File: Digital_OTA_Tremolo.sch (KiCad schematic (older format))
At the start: 25 parts

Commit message: updates
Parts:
- added R?: 10K, symbol Device:R
- added RV?: 47K, symbol Device:R_POT_TRIM
- R?: value 33K -> 4K7
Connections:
- net labels added: CV
- net labels removed: DAC1
- wire segments 95 -> 106
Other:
- moved on the sheet: R?
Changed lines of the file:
@@
 L Digital_OTA_Tremolo-rescue:R R?
 U 1 1 5AD2DE34
-P 6200 3800
-F 0 "R?" V 6280 3800 50  0000 C CNN
-F 1 "33K" V 6200 3800 50  0000 C CNN
-F 2 "" V 6130 3800 50  0001 C CNN
-F 3 "" H 6200 3800 50  0001 C CNN
-	1    6200 3800
+P 5825 3800
+F 0 "R?" V 5905 3800 50  0000 C CNN
+F 1 "4K7" V 5825 3800 50  0000 C CNN
+F 2 "" V 5755 3800 50  0001 C CNN
+F 3 "" H 5825 3800 50  0001 C CNN
+	1    5825 3800
 	0    1    1    0
 $EndComp
@@
 	10900 3500 11450 3500
 Wire Wire Line
-	5400 3800 6050 3800
+	5400 3800 5675 3800
 $Comp
 L Device:R_POT_TRIM RV?
@@
 	9550 3500 9900 3500
 Wire Wire Line
-	8825 3500 9550 3500
+	8825 3500 9275 3500
 Wire Wire Line
 	10200 3800 10200 3975
@@
 	1    0    0    -1
 $EndComp
-Wire Wire Line
-	6350 3800 6900 3800
-Connection ~ 6900 3800
 $Comp
 L Device:D D?
@@
 Wire Wire Line
 	11750 3500 12300 3500
-Wire Wire Line
-	8825 3600 9025 3600
 $Comp
 L MCU_ST_STM32F0:STM32F051K8Tx U?
@@
 $EndComp
 Wire Wire Line
-	4525 6875 9025 6875
-Wire Wire Line
-	9025 6875 9025 3600
-Text Label 6025 6875 0    50   ~ 0
-DAC1
-Text Notes 6025 6975 0    50   ~ 0
+	4525 6875 5500 6875
+Text Notes 4650 6975 0    50   ~ 0
 SINE WAVE < 30Hz\n
 $Comp
@@
 Wire Wire Line
 	6525 7575 6525 7275
+Wire Wire Line
+	6900 3200 6175 3200
+Wire Wire Line
+	6175 3200 6175 3800
+Wire Wire Line
+	6175 3800 5975 3800
+Connection ~ 6900 3200
+Wire Wire Line
+	8825 3600 9075 3600
+Text Label 9075 3600 2    50   ~ 0
+CV
+Text Label 6475 6875 2    50   ~ 0
+CV
+Wire Wire Line
+	9275 3500 9275 4350
+Wire Wire Line
+	9275 4350 8850 4350
+Wire Wire Line
+	8100 4350 8100 3800
+Connection ~ 9275 3500
+Wire Wire Line
+	9275 3500 9550 3500
+Connection ~ 8100 3800
+$Comp
+L Device:R R?
+U 1 1 5E90DE19
+P 8700 4350
+F 0 "R?" V 8493 4350 50  0000 C CNN
+F 1 "10K" V 8584 4350 50  0000 C CNN
+F 2 "" V 8630 4350 50  0001 C CNN
+F 3 "~" H 8700 4350 50  0001 C CNN
+	1    8700 4350
+	0    1    1    0
+$EndComp
+Wire Wire Line
+	8550 4350 8100 4350
+$Comp
+L Device:R_POT_TRIM RV?
+U 1 1 5E9351EC
+P 5875 6875
+F 0 "RV?" V 5760 6875 50  0000 C CNN
+F 1 "47K" V 5669 6875 50  0000 C CNN
+F 2 "" H 5875 6875 50  0001 C CNN
+F 3 "~" H 5875 6875 50  0001 C CNN
+	1    5875 6875
+	0    -1   -1   0
+$EndComp
+Wire Wire Line
+	6025 6875 6475 6875
+Wire Wire Line
+	5875 6725 5875 6675
+Wire Wire Line
+	5875 6675 5500 6675
+Wire Wire Line
+	5500 6675 5500 6875
+Connection ~ 5500 6875
+Wire Wire Line
+	5500 6875 5725 6875
 $EndSCHEMATC

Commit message: updates
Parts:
- removed R? (x2): 10k, symbol Device:R
- removed RV?: 47K, symbol Device:R_POT_TRIM
- removed SW?: Rotary_Encoder, symbol Device:Rotary_Encoder
- removed U? (x2): LM833, symbol Digital_OTA_Tremolo-rescue:TL074
- removed U?: STM32F051K8Tx, Package_QFP:LQFP-32_7x7mm_P0.8mm, symbol MCU_ST_STM32F0:STM32F051K8Tx
- added C? (x4): C, symbol Device:C
- added D?: 1N914, symbol Device:D
- added D? (x2): LED, symbol Device:LED
- added R? (x3): 10K, symbol Digital_OTA_Tremolo-rescue:R
- added R? (x2): 10K, symbol Device:R
- added R?: 33K, symbol Digital_OTA_Tremolo-rescue:R
- added R?: 4K7, symbol Digital_OTA_Tremolo-rescue:R
- added R? (x3): 1K, symbol Digital_OTA_Tremolo-rescue:R
- added R? (x2): 1K, symbol Device:R
- added R? (x2): 2K7, symbol Digital_OTA_Tremolo-rescue:R
- added R? (x2): 33K, symbol Device:R
- added RV? (x2): B10K, symbol Device:R_POT
- added U? (x6): TL072, symbol Amplifier_Operational:TL072
- added U?: STM32F072RBTx, Package_QFP:LQFP-64_10x10mm_P0.5mm, symbol MCU_ST_STM32F0:STM32F072RBTx
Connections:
- net labels added: +3V3, CV1, CV2, INV_CV1, INV_CV2, InvertInput, NonInvInput, RATE1, RATE2
- net labels removed: CV
- wire segments 106 -> 194
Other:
- note added: "3.7 Gain"
- note added: "DAC: Channel 1 + 2\nSINE WAVE < 100Hz\n"
- note removed: "SINE WAVE < 30Hz\n"
- moved on the sheet: C?, D?, J?, R?, RV?, U?, U?A, U?B, U?C, U?D

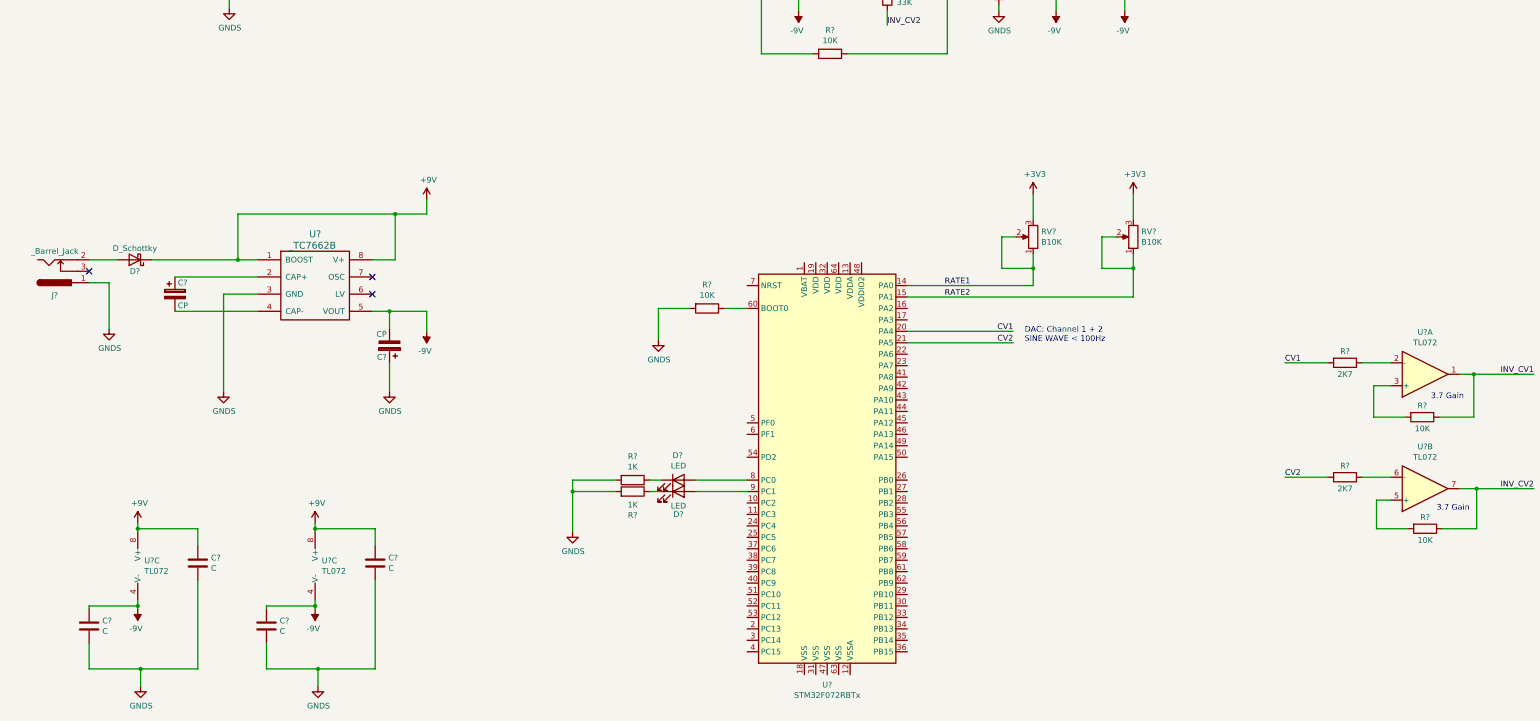
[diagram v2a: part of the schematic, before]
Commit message: updated schema
_ added controls
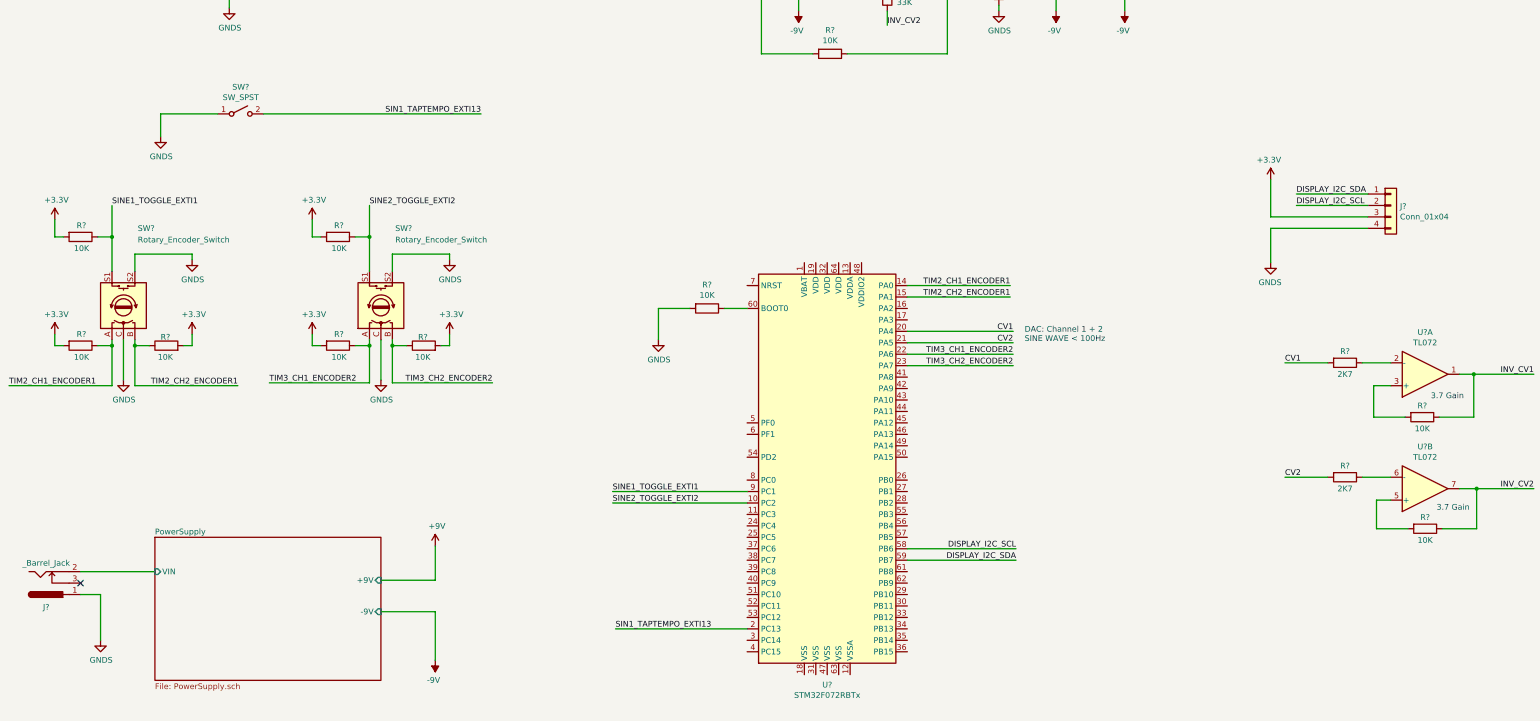
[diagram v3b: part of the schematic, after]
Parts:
- removed C? (x2): CP, symbol Digital_OTA_Tremolo-rescue:CP
- removed C? (x4): C, symbol Device:C
- removed D?: D_Schottky, symbol Digital_OTA_Tremolo-rescue:D_Schottky
- removed D? (x2): LED, symbol Device:LED
- removed J?: _Barrel_Jack, symbol barrel_jack:_Barrel_Jack
- removed R? (x2): 1K, symbol Device:R
- removed RV? (x2): B10K, symbol Device:R_POT
- removed U?: _TC7662B, symbol _TC7662b:_TC7662B
- removed U? (x2): TL072, symbol Amplifier_Operational:TL072
- added J?: _Barrel_Jack, symbol barrel_jack:_Barrel_Jack
- added J?: Conn_01x04, symbol Connector_Generic:Conn_01x04
- added R? (x6): 10K, symbol Device:R
- added SW? (x2): Rotary_Encoder_Switch, symbol Device:Rotary_Encoder_Switch
- added SW?: SW_SPST, symbol Switch:SW_SPST
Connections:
- net +3V3: now also J?.3 (Pin_3), R?.2, R?.2, R?.2, R?.2, R?.2, R?.2
- net GNDS: now also J?.1, J?.4 (Pin_4), SW?.1 (A), SW?.C, SW?.C, SW?.S2, SW?.S2
- net SINE1_TOGGLE_EXTI1: now reaches U?.9 (PC1)
- net SINE1_TOGGLE_EXTI1: now also R?.1, SW?.S1
- net SINE2_TOGGLE_EXTI2: now reaches U?.10 (PC2)
- net SINE2_TOGGLE_EXTI2: now also R?.1, SW?.S1
- net SIN1_TAPTEMPO_EXTI13: now reaches U?.2 (PC13)
- net SIN1_TAPTEMPO_EXTI13: now also SW?.2 (B)
- net TIM3_CH1_ENCODER2: now reaches U?.22 (PA6)
- net TIM3_CH1_ENCODER2: now also R?.1, SW?.A
- net TIM3_CH2_ENCODER2: now reaches U?.23 (PA7)
- net TIM3_CH2_ENCODER2: now also R?.1, SW?.B
- net DISPLAY_I2C_SCL: now reaches U?.58 (PB6)
- net DISPLAY_I2C_SCL: now also J?.2 (Pin_2)
- net DISPLAY_I2C_SDA: now reaches U?.59 (PB7)
- net DISPLAY_I2C_SDA: now also J?.1 (Pin_1)
- net RATE1 renamed TIM2_CH1_ENCODER1
- net TIM2_CH1_ENCODER1: now also R?.1, SW?.A
- net RATE2 renamed TIM2_CH2_ENCODER1
- net TIM2_CH2_ENCODER1: now also R?.1, SW?.B
- new net PowerSupply/VIN: J?.2
- no-connect marks 5 -> 3

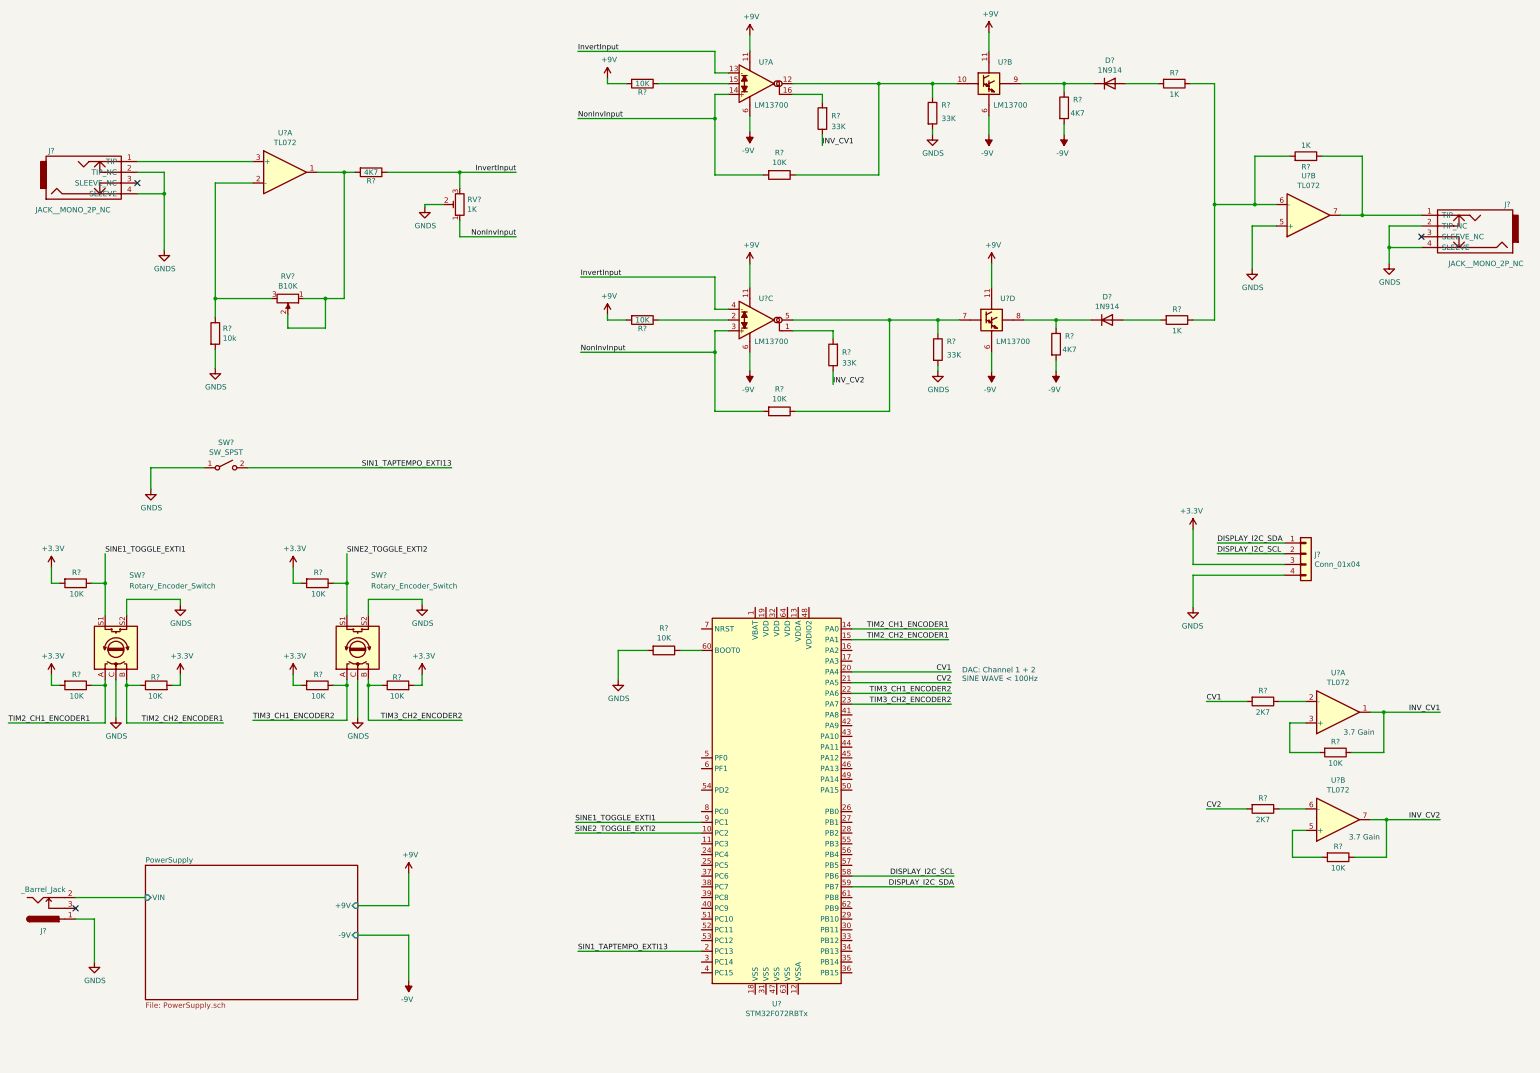
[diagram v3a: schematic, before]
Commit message: Updated power supply section
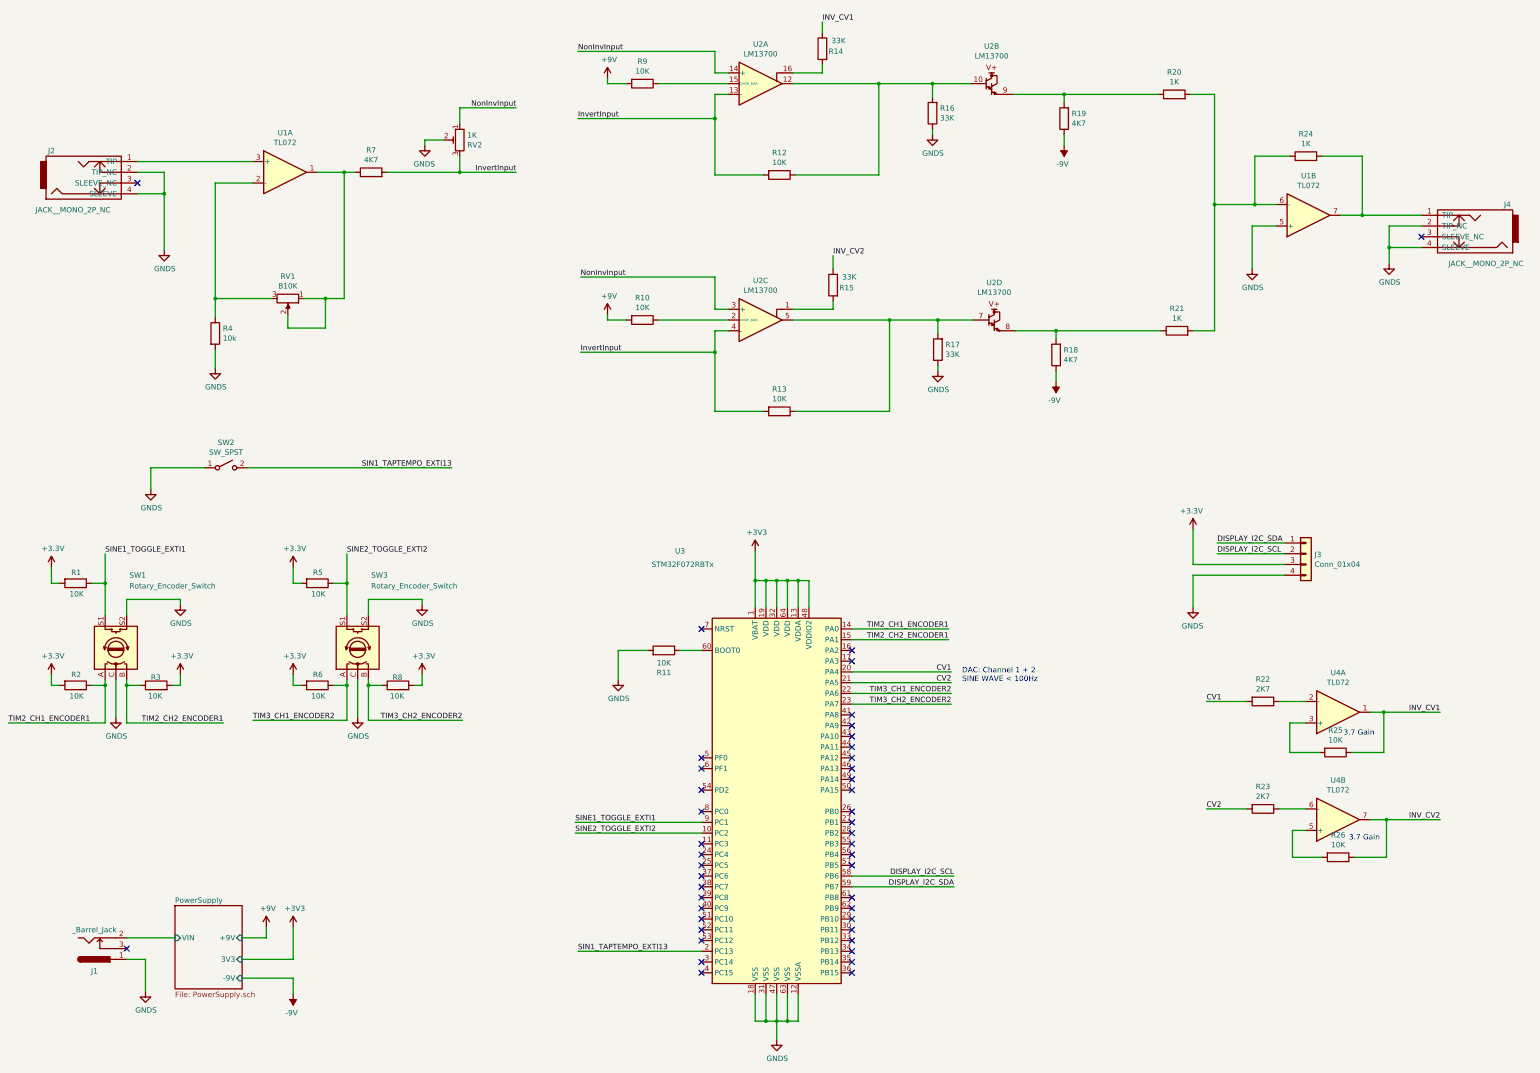
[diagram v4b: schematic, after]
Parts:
- removed D? (x2): 1N914, symbol Device:D
- removed R? (x4): 10K, symbol Digital_OTA_Tremolo-rescue:R
- removed R? (x3): 4K7, symbol Digital_OTA_Tremolo-rescue:R
- removed R? (x2): 33K, symbol Digital_OTA_Tremolo-rescue:R
- removed R? (x3): 1K, symbol Digital_OTA_Tremolo-rescue:R
- removed R? (x2): 2K7, symbol Digital_OTA_Tremolo-rescue:R
- removed U? (x4): LM13700, symbol Digital_OTA_Tremolo-rescue:LM13700
- added R10, R25, R26, R9: 10K, symbol Device:R
- added R16, R17: 33K, symbol Device:R
- added R18, R19, R7: 4K7, symbol Device:R
- added R20, R21, R24: 1K, symbol Device:R
- added R22, R23: 2K7, symbol Device:R
- added U2: LM13700, symbol Amplifier_Operational:LM13700
- gave numbers to parts that had none: 24
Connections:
- net +3V3: now also U3.1 (VBAT), U3.13 (VDDA), U3.19 (VDD), U3.32 (VDD), U3.48 (VDDIO2), U3.64 (VDD)
- net +9V: now also R10.2, R9.2
- net -9V: now also R18.1, R19.1
- net CV1: now also R22.2
- net CV2: now also R23.2
- net GNDS: now also U3.12 (VSSA), U3.18 (VSS), U3.31 (VSS), U3.47 (VSS), U3.63 (VSS), R16.1, R17.1
- net INV_CV1: now also R25.1
- net INV_CV2: now also R26.1
- net InvertInput: now also R12.2, R13.2, R7.2, U2.13 (-), U2.4 (-)
- net NonInvInput: now also U2.14 (+), U2.3 (+); no longer R12.2, R13.2
- net at R12.1: now also R16.2, U2.10, U2.12
- net at R14.2: now also U2.16
- net at R15.2: now also U2.1
- net at R13.1: now also R17.2, U2.5, U2.7
- net at J4.1 (TIP), U1.7: now also R24.2
- net at RV1.1, RV1.2, U1.1: now also R7.1
- net at U1.6 (-): now also R20.2, R21.2, R24.1
- net at U4.2 (-): now also R22.1
- net at U4.3 (+): now also R25.2
- net at U4.5 (+): now also R26.2
- net at U4.6 (-): now also R23.1
- new net: R9.1, U2.15 (DIODE_BIAS)
- new net: R19.2, R20.1, U2.9
- new net: R10.1, U2.2 (DIODE_BIAS)
- new net: R18.2, R21.1, U2.8
- no-connect marks 3 -> 44
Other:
- moved on the sheet: J1, R14, R15, RV2

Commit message: Updated RevA design
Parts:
- removed J1: _Barrel_Jack, symbol barrel_jack:_Barrel_Jack
- removed J2, J4: JACK__MONO_2P_NC, symbol socket_custom:JACK__MONO_2P_NC
- removed RV1: B10K, symbol pot_numbered:NPOT
- removed U1, U4: TL072, symbol Amplifier_Operational:TL072
- added J1, J4: NRJ6HM-1-PRE, NeutrikNRJ:NRJxHx, symbol MonoJack2Switch:MonoJack2Switch
- added J2: Barrel_Jack_Switch, Connector_BarrelJack:BarrelJack_Horizontal, symbol Connector:Barrel_Jack_Switch
- added RV1: B10K, Potentiometer_THT:Potentiometer_Bourns_PTV09A-1_Single_Vertical, symbol Device:R_POT
- added U1: TL074, Package_SO:SOIC-16_3.9x9.9mm_P1.27mm, symbol Amplifier_Operational:TL074
- J3: footprint (none) -> Connector_Molex:Molex_KK-254_AE-6410-04A_1x04_P2.54mm_Vertical
- R1, R10, R11, R12, R13, R14, R15, R16, R17, R18, R19, R2, R20, R21, R22, R23, R24, R25, R26, R3, R4, R5, R6, R7, R8, R9: footprint (none) -> Resistor_SMD:R_0805_2012Metric_Pad1.15x1.40mm_HandSolder
- RV2: footprint (none) -> Potentiometer_SMD:Potentiometer_Bourns_3314J_Vertical
- SW1, SW3: footprint (none) -> Rotary_Encoder:RotaryEncoder_Alps_EC11E-Switch_Vertical_H20mm
- SW2: footprint (none) -> Connector_Molex:Molex_KK-254_AE-6410-02A_1x02_P2.54mm_Vertical
- U2: footprint (none) -> Package_SO:SOIC-16_3.9x9.9mm_P1.27mm
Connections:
- net INV_CV1: now also U1.8
- net INV_CV2: now also U1.14
- net at R24.2: now also J4.1 (TIP), U1.7
- net at R4.1: now also RV1.3, U1.2 (-)
- net at R7.1: now also RV1.1, RV1.2, U1.1
- net at R20.2, R21.2, R24.1: now also U1.6 (-)
- net at R26.2: now also U1.12 (+)
- net at R25.2: now also U1.10 (+)
- net at R22.1: now also U1.9 (-)
- net at R23.1: now also U1.13 (-)
- net +9V renamed +15V
- net -9V renamed -15V
- net GNDS renamed VCOM
- net VCOM: now also J1.2 (TIP_NC), J1.3 (SLEEVE_NC), J1.4 (SLEEVE), J4.2 (TIP_NC), J4.3 (SLEEVE_NC), J4.4 (SLEEVE), U1.5 (+)
- new net: J1.1 (TIP), U1.3 (+)
- new net PowerSupply/+VIN: J2.2
- new net PowerSupply/-VIN: J2.1
- no-connect marks 44 -> 42
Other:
- note added: "+9V\nCenter Negative"
- moved on the sheet: J3, R1, R2, R22, R23, R25, R26, R3, R4, R5, R6, R7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

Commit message: Added switching mechanism
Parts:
- added D5, D6: LED, LED_THT:LED_D5.0mm-4_RGB_Wide_Pins, symbol Device:LED
- added R30, R31: 1K, Resistor_SMD:R_0805_2012Metric_Pad1.15x1.40mm_HandSolder, symbol Device:R
- added SW_BYPASS1: SW_SPST, Connector_Molex:Molex_KK-254_AE-6410-02A_1x02_P2.54mm_Vertical, symbol Switch:SW_SPST
- added U4, U7, U8: DG468DV_T1_E3, Package_TO_SOT_SMD:SOT-23-6_Handsoldering, symbol DG46x:DG468DV_T1_E3
- renumbered SW2 to SW_TAP1
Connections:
- net +15V: now also U4.5 (V+), U7.5 (V+), U8.5 (V+)
- net -15V: now also U4.2 (V-), U7.2 (V-), U8.2 (V-)
- net VCOM: now also D5.1 (K), D6.1 (K), SW_BYPASS1.1 (A), U4.4 (GND), U7.4 (GND), U8.4 (GND)
- net at R24.2, U1.7: now also U8.1 (NO); no longer J4.1 (TIP)
- net at J1.1 (TIP): now also U4.1 (NO), U7.1 (NO); no longer U1.3 (+)
- net SW_BYPASS_EXTI3: now reaches U3.11 (PC3)
- net SW_BYPASS_EXTI3: now also SW_BYPASS1.2 (B)
- net SW_CLOSE_FX: now reaches U3.24 (PC4)
- net SW_CLOSE_FX: now also U4.3 (IN), U8.3 (IN)
- net SW_CLOSE_BYPASS: now reaches U3.25 (PC5)
- net SW_CLOSE_BYPASS: now also U7.3 (IN)
- net SINE1_LED: now reaches U3.37 (PC6)
- net SINE1_LED: now also R30.2
- net SINE2_LED: now reaches U3.38 (PC7)
- net SINE2_LED: now also R31.2
- net DISPLAY_I2C_SCL renamed DISPLAY_I2C1_SCL
- net DISPLAY_I2C_SDA renamed DISPLAY_I2C1_SDA
- net SIN1_TAPTEMPO_EXTI13 renamed SINE1_TAPTEMPO_EXTI13
- new net: U1.3 (+), U4.6 (COM)
- new net: J4.1 (TIP), U7.6 (COM), U8.6 (COM)
- new net: D5.2 (A), R30.1
- new net: D6.2 (A), R31.1
- no-connect marks 42 -> 37
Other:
- moved on the sheet: J1, J2, J3, J4, R1, R10, R11, R12, R13, R14, R15, R16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

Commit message: updated readme
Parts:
- D5, D6: footprint LED_THT:LED_D5.0mm-4_RGB_Wide_Pins -> LED_SMD:LED_1206_3216Metric_Pad1.42x1.75mm_HandSolder
